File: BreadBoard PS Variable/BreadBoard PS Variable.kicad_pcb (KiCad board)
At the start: 2 copper layers, 29.8 x 52 mm, 19 parts, among them J1 Barrel_Jack_Switch_MountingPin, J2 Conn_02x02_Odd_Even, J3 Conn_02x02_Odd_Even, J4 Conn_02x02_Odd_Even, J5 Conn_02x02_Odd_Even, SW1 SW_SPDT, U1 LM317T

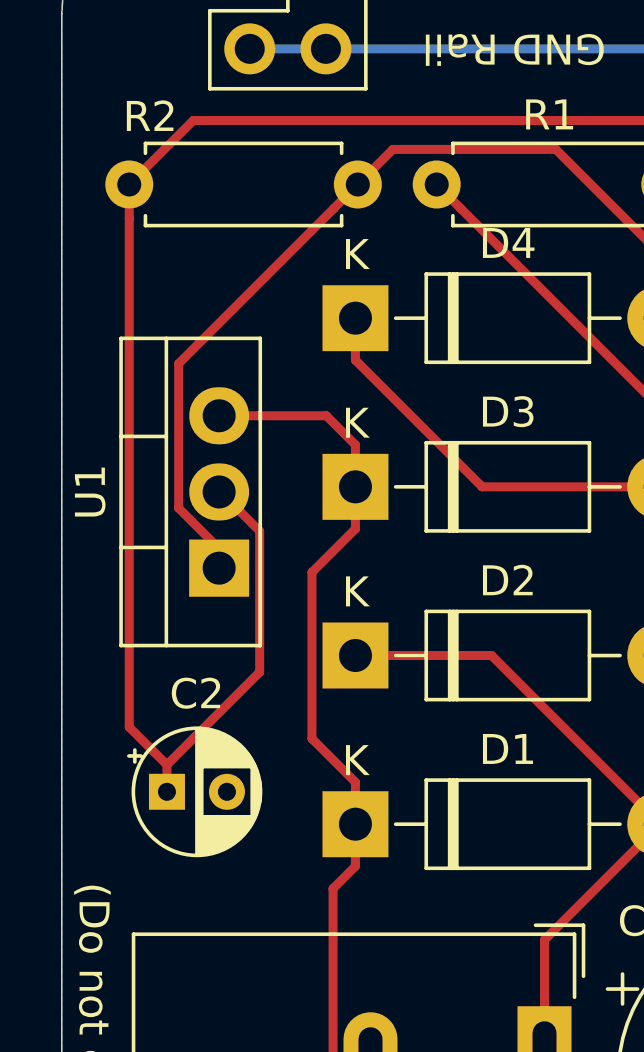
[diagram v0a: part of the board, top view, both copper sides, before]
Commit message: correct C2 foot print
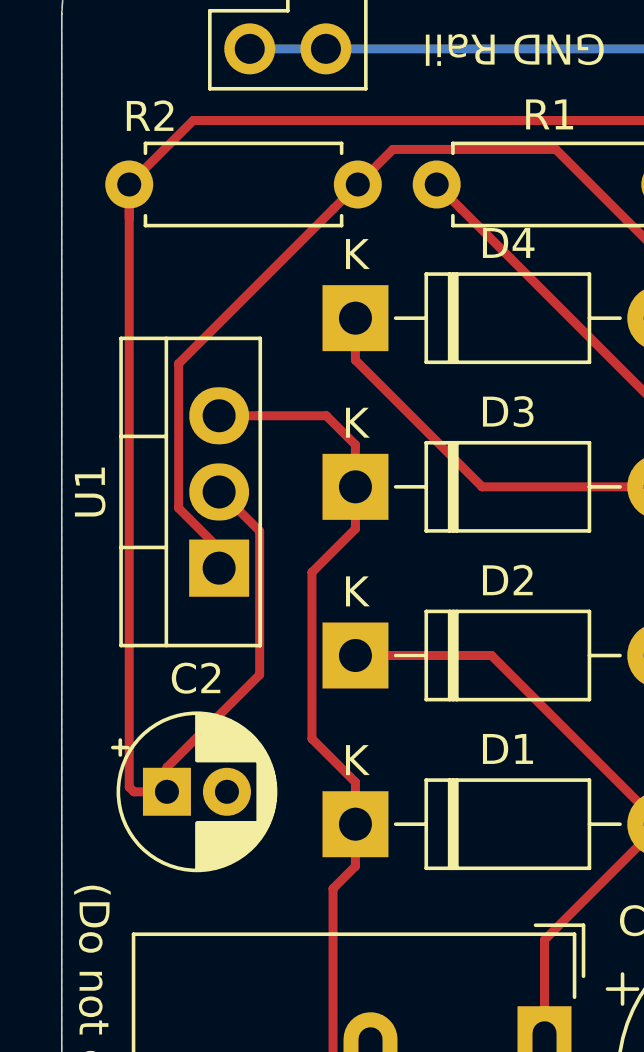
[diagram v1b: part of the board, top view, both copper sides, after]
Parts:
- C2: footprint Capacitor_THT:CP_Radial_D4.0mm_P2.00mm -> Capacitor_THT:CP_Radial_D5.0mm_P2.00mm
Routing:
- net /Vari-V: track 58.3 -> 61.0 mm
